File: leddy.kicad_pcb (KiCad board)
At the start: 4 copper layers, 83 x 61 mm, 98 parts, among them J1 hole 1, J2 hole 1, J3 hole 1, J4 hole 1, J5 umbrella hole, J6 PJ-002AH-SMT-TR, J7 OPEN HARDWARE, Q1 ZXMP6A13GTA, SW1 PTS645SM70SMTR92, U1 LT3518EFE#PBF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

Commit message: added better LED current level meter
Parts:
- added C6: 0.1uF, Capacitors_SMD:C_0603_HandSoldering, B.Cu at (145.5, 91.7)
- added J8: label_power-in, lib:Polarity_Center_Positive_3mm_SilkScreen, F.Cu at (149.5, 55.0)
- added R14: 0R, Resistors_SMD:R_0603_HandSoldering, B.Cu at (145.5, 88.7)
- added R15: 0R, Resistors_SMD:R_0603_HandSoldering, B.Cu at (145.5, 84.7)
- added R16: 0R, Resistors_SMD:R_0603_HandSoldering, B.Cu at (145.5, 80.7)
- added R17: 0R, Resistors_SMD:R_0603_HandSoldering, B.Cu at (145.5, 76.7)
- D51: value 29.9V -> 30V; moved to B.Cu
- D52, D55, D56, D57, D58, J6, R13, SW1: moved to B.Cu
- D53: value 24.2V -> 24V; moved to B.Cu
- D54: value 22.4V -> 22V; moved to B.Cu
- R12: value 1M -> 30.1k
- moved D53 54.1 mm to (136.0, 80.7)
- moved R13 54.1 mm to (140.0, 91.7)
- moved D58 53.9 mm to (140.5, 76.7), turned to 180 degrees
- moved D55 51.3 mm to (140.5, 88.7), turned to 180 degrees
- moved D54 49.3 mm to (136.0, 76.7)
- moved D52 48.4 mm to (136.0, 84.7)
- moved D57 47.0 mm to (140.5, 80.7), turned to 180 degrees
- moved D51 42.7 mm to (136.0, 88.7)
- moved D56 40.3 mm to (140.5, 84.7), turned to 180 degrees
- moved J6 1.75 mm to (145.8, 53.5)
- moved SW1 1.50 mm to (138.0, 102.0), turned to 90 degrees
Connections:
- D55 pad 1: GND -> Net-(D55-Pad1)
- D56 pad 1: GND -> Net-(D56-Pad1)
- D57 pad 1: GND -> Net-(D57-Pad1)
- D58 pad 1: GND -> Net-(D58-Pad1)
- U1 pad 12: Net-(R1-Pad2) -> Net-(Q1-Pad3)

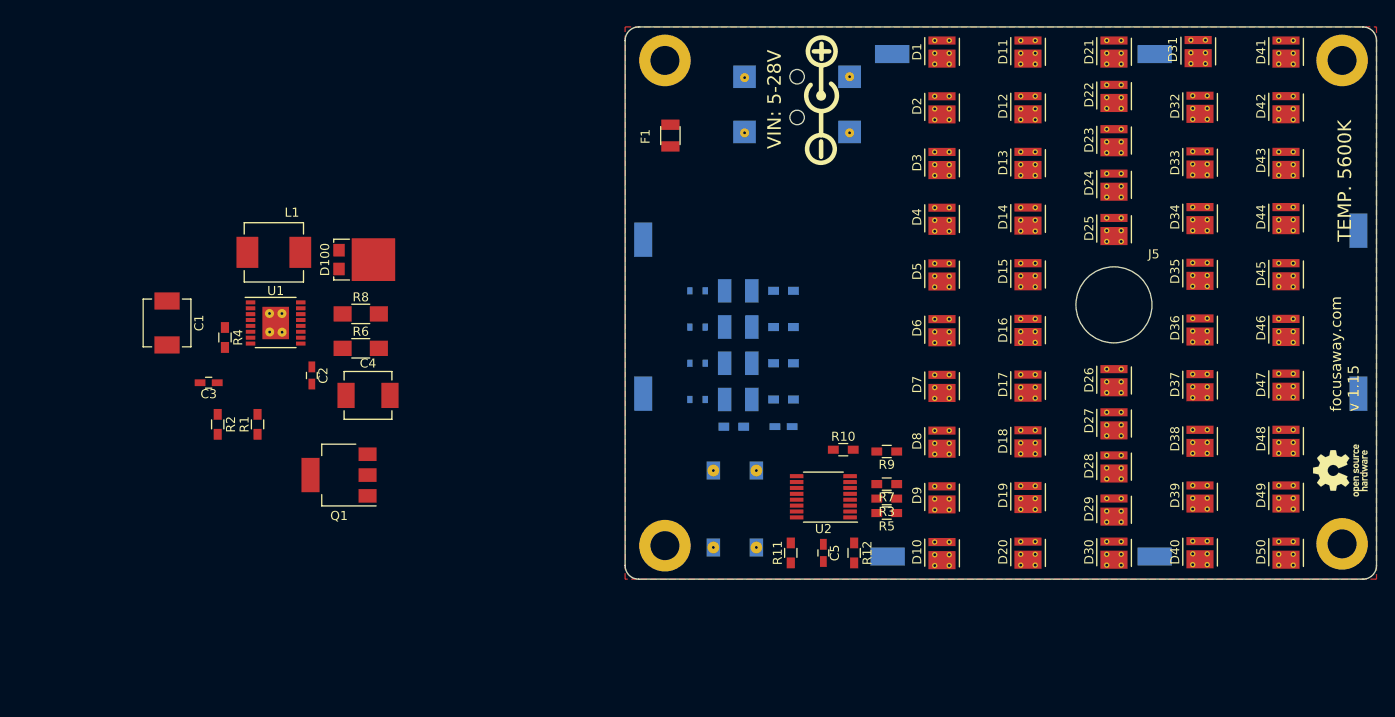
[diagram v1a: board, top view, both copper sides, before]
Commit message: total power is now 60W and there are 6 level of led power regulation
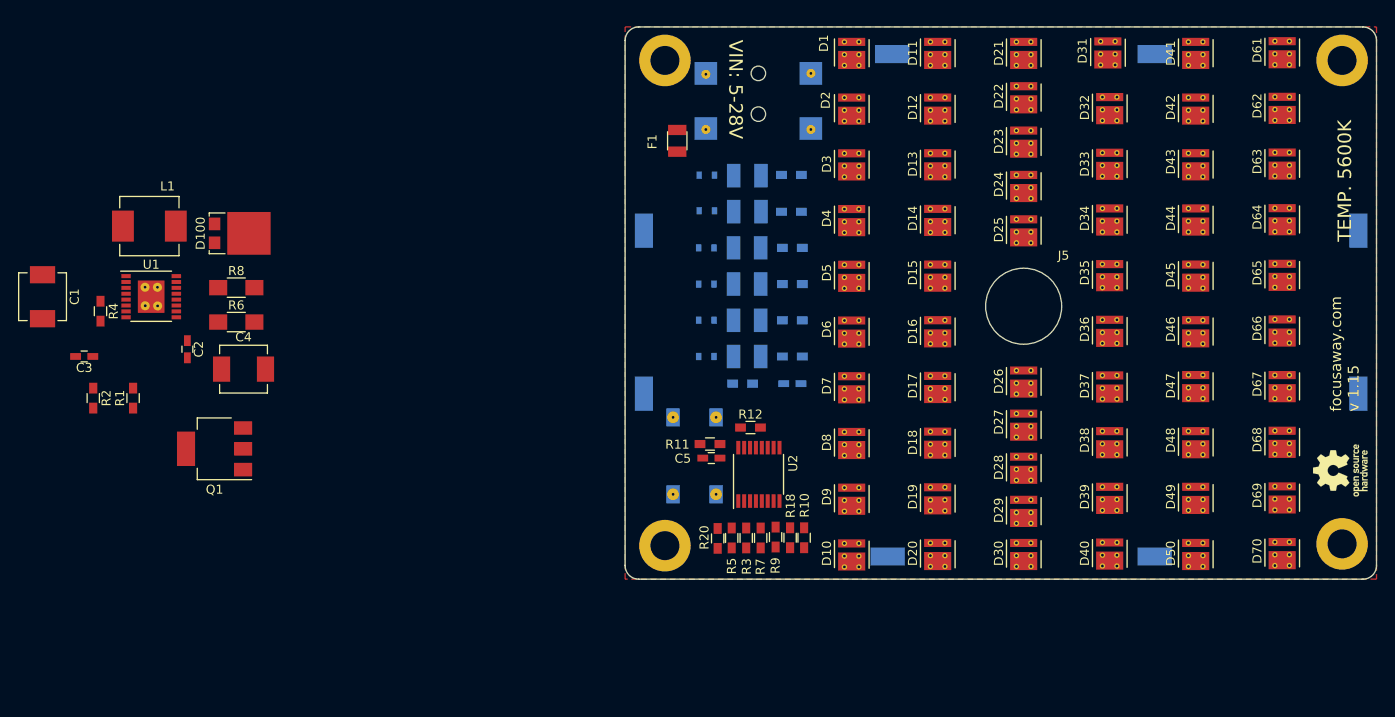
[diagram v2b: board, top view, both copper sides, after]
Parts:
- removed J8: label_power-in, lib:Polarity_Center_Positive_3mm_SilkScreen
- added D59: 20V, Diodes_SMD:D_0603, B.Cu at (137.0, 67.8)
- added D60: LED, lib:LED_PLCC-2, B.Cu at (141.5, 67.9)
- added D61: LED, lib:LED-3030, F.Cu at (200.6, 50.0)
- added D62: LED, lib:LED-3030, F.Cu at (200.6, 56.1)
- added D63: LED, lib:LED-3030, F.Cu at (200.6, 62.3)
- added D64: LED, lib:LED-3030, F.Cu at (200.6, 68.4)
- added D65: LED, lib:LED-3030, F.Cu at (200.6, 74.6)
- added D66: LED, lib:LED-3030, F.Cu at (200.6, 80.7)
- added D67: LED, lib:LED-3030, F.Cu at (200.6, 86.9)
- added D68: LED, lib:LED-3030, F.Cu at (200.6, 93.0)
- added D69: LED, lib:LED-3030, F.Cu at (200.6, 99.2)
- added D70: LED, lib:LED-3030, F.Cu at (200.6, 105.3)
- added D71: 18V, Diodes_SMD:D_0603, B.Cu at (137.0, 63.9)
- added D72: LED, lib:LED_PLCC-2, B.Cu at (141.5, 63.9)
- added R18: 50k, Resistors_SMD:R_0603_HandSoldering, F.Cu at (147.8, 103.9)
- added R19: 0R, Resistors_SMD:R_0603_HandSoldering, B.Cu at (146.4, 67.9)
- added R20: 60k, Resistors_SMD:R_0603_HandSoldering, F.Cu at (138.2, 104.0)
- added R21: 0R, Resistors_SMD:R_0603_HandSoldering, B.Cu at (146.4, 63.9)
- moved R12 18.0 mm to (141.8, 91.8), turned to 0 degrees
- moved R5 17.3 mm to (139.8, 104.0), turned to 90 degrees
- moved C5 16.2 mm to (137.5, 95.1), turned to 180 degrees
- moved R3 16.1 mm to (141.4, 104.0), turned to 90 degrees
- moved R9 15.5 mm to (144.6, 103.8), turned to 90 degrees
- moved R7 15.1 mm to (143.0, 104.0), turned to 90 degrees
- moved R11 15.0 mm to (137.4, 93.6), turned to 0 degrees
- moved C1 14.1 mm to (63.6, 77.3)
- moved C2 14.1 mm to (79.7, 83.1)
- moved C4 14.1 mm to (85.8, 85.3)
- moved D100 14.1 mm to (84.5, 70.3)
- moved L1 14.1 mm to (75.5, 69.5)
- moved Q1 14.1 mm to (82.7, 94.1)
- moved R1 14.1 mm to (73.7, 88.5)
- moved R2 14.1 mm to (69.2, 88.5)
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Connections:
- C1 pad 1: Net-(C1-Pad1) -> Vin
- F1 pad 1: Net-(C1-Pad1) -> Vin
- F1 pad 2: Vin -> Net-(F1-Pad2)
- J6 pad 1: Vin -> Net-(F1-Pad2)
- L1 pad 1: Net-(C1-Pad1) -> Vin
- U1 pad 13: Net-(U1-Pad13) -> VLED
- U1 pad 3: Net-(C1-Pad1) -> Vin
- U1 pad 4: Net-(C1-Pad1) -> Vin
- U2 pad 10: Net-(U2-Pad10) -> Net-(R18-Pad2)
- U2 pad 15: Net-(U2-Pad10) -> Net-(U2-Pad15)
- U2 pad 5: Net-(U2-Pad5) -> Net-(U2-Pad15)

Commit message: pcb rounted
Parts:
- moved C1 79.8 mm to (142.8, 87.9), turned to 0 degrees
- moved R2 79.1 mm to (147.9, 79.7)
- moved C3 78.6 mm to (146.8, 82.5), turned to 0 degrees
- moved R1 75.4 mm to (147.9, 75.6), turned to 270 degrees
- moved R4 74.6 mm to (144.4, 84.2), turned to 0 degrees
- moved C2 66.5 mm to (145.9, 77.0)
- moved U1 66.4 mm to (142.0, 79.6), turned to 90 degrees
- moved C4 63.4 mm to (145.5, 63.7), turned to 180 degrees
- moved R6 61.4 mm to (146.0, 72.1), turned to 180 degrees
- moved R8 61.2 mm to (145.9, 69.6), turned to 180 degrees
- moved L1 60.7 mm to (135.1, 80.4), turned to 90 degrees
- moved Q1 59.7 mm to (137.9, 71.5)
- moved D100 54.5 mm to (138.8, 64.7), turned to 180 degrees
- moved R15 4.33 mm to (142.6, 81.8)
- moved C6 4.27 mm to (142.3, 87.6)
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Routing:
- net Vin: track 0.00 -> 201.7 mm, vias 0 -> 14
- net VLED: track 0.00 -> 119.6 mm, vias 0 -> 8
- net GND: track 0.00 -> 77.5 mm, vias 0 -> 28
- net CTRL: track 0.00 -> 47.7 mm, vias 0 -> 2
- net Net-(D51-Pad1): track 0.00 -> 24.7 mm
- net Net-(D25-Pad1): track 0.00 -> 20.4 mm
- net Net-(C5-Pad1): track 0.00 -> 16.3 mm, vias 0 -> 2
- net Net-(D100-Pad2): track 0.00 -> 16.0 mm
- net Net-(R12-Pad2): track 0.00 -> 15.7 mm, vias 0 -> 1
- net Vref: track 0.00 -> 12.4 mm
- net Net-(Q1-Pad3): track 0.00 -> 11.0 mm
- net Net-(R18-Pad2): track 0.00 -> 10.3 mm
- net Net-(F1-Pad2): track 0.00 -> 9.28 mm
- net Net-(U2-Pad15): track 0.00 -> 6.71 mm
- net Net-(C2-Pad1): track 0.00 -> 4.49 mm
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- added copper zone on B.Cu, net GND
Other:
- copper layers 4 -> 2
